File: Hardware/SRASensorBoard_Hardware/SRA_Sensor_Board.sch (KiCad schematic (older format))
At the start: 15 parts, among them U1 OKI-78SR-5_1.5-W36H-C, U2 OKI-78SR-3.3_1.5-W36H-C

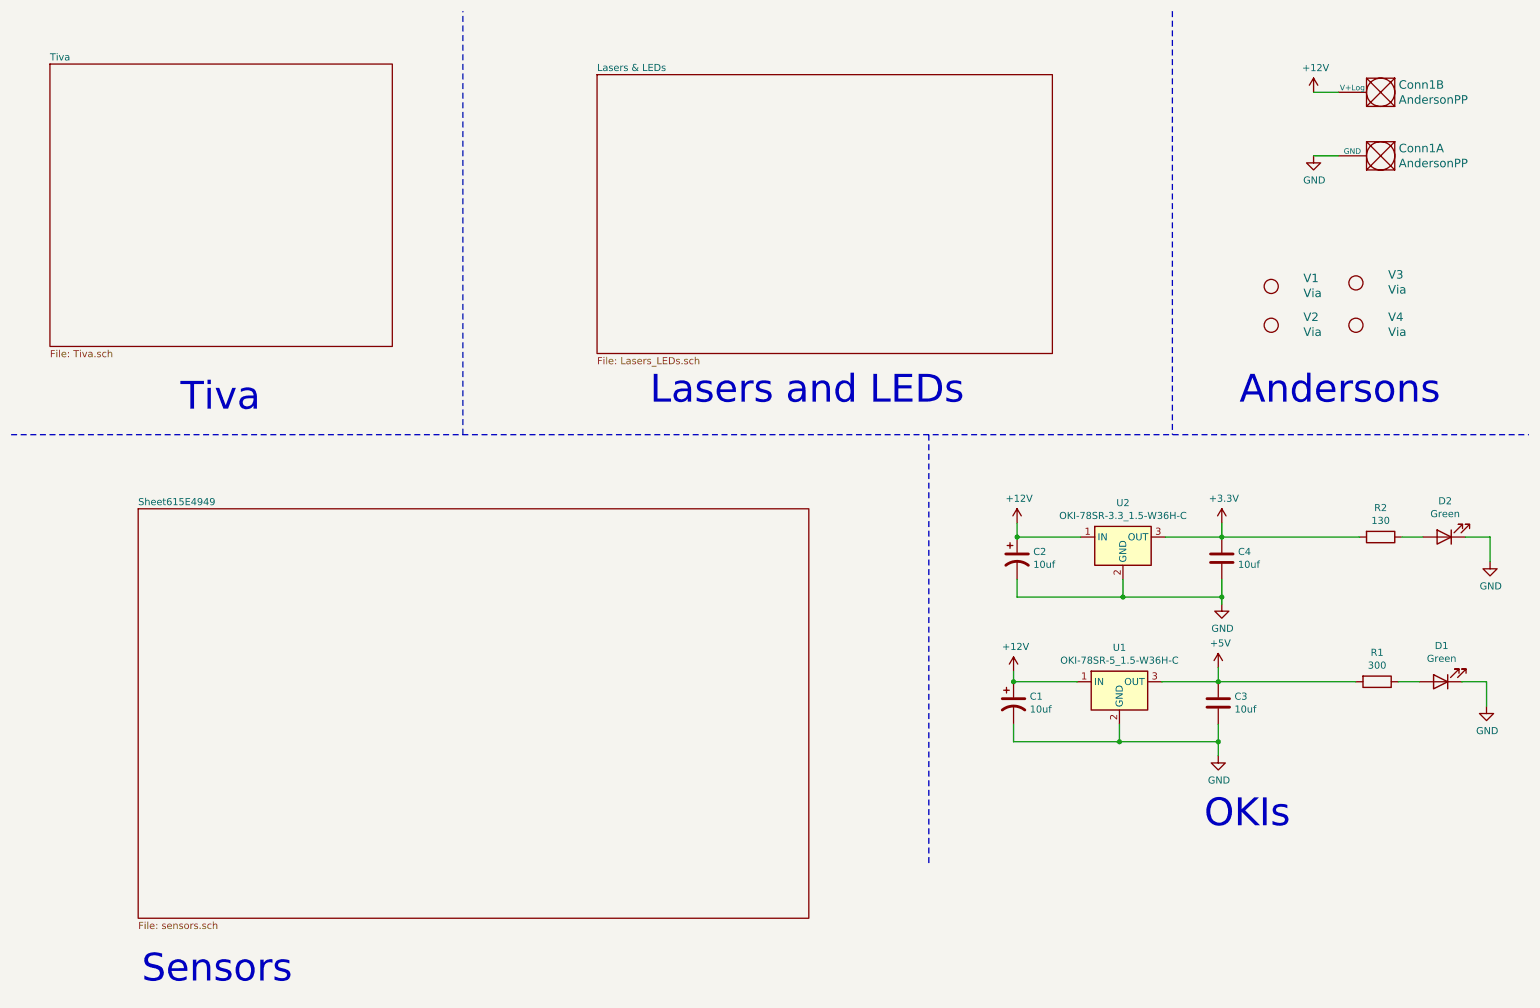
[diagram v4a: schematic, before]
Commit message: added teensy
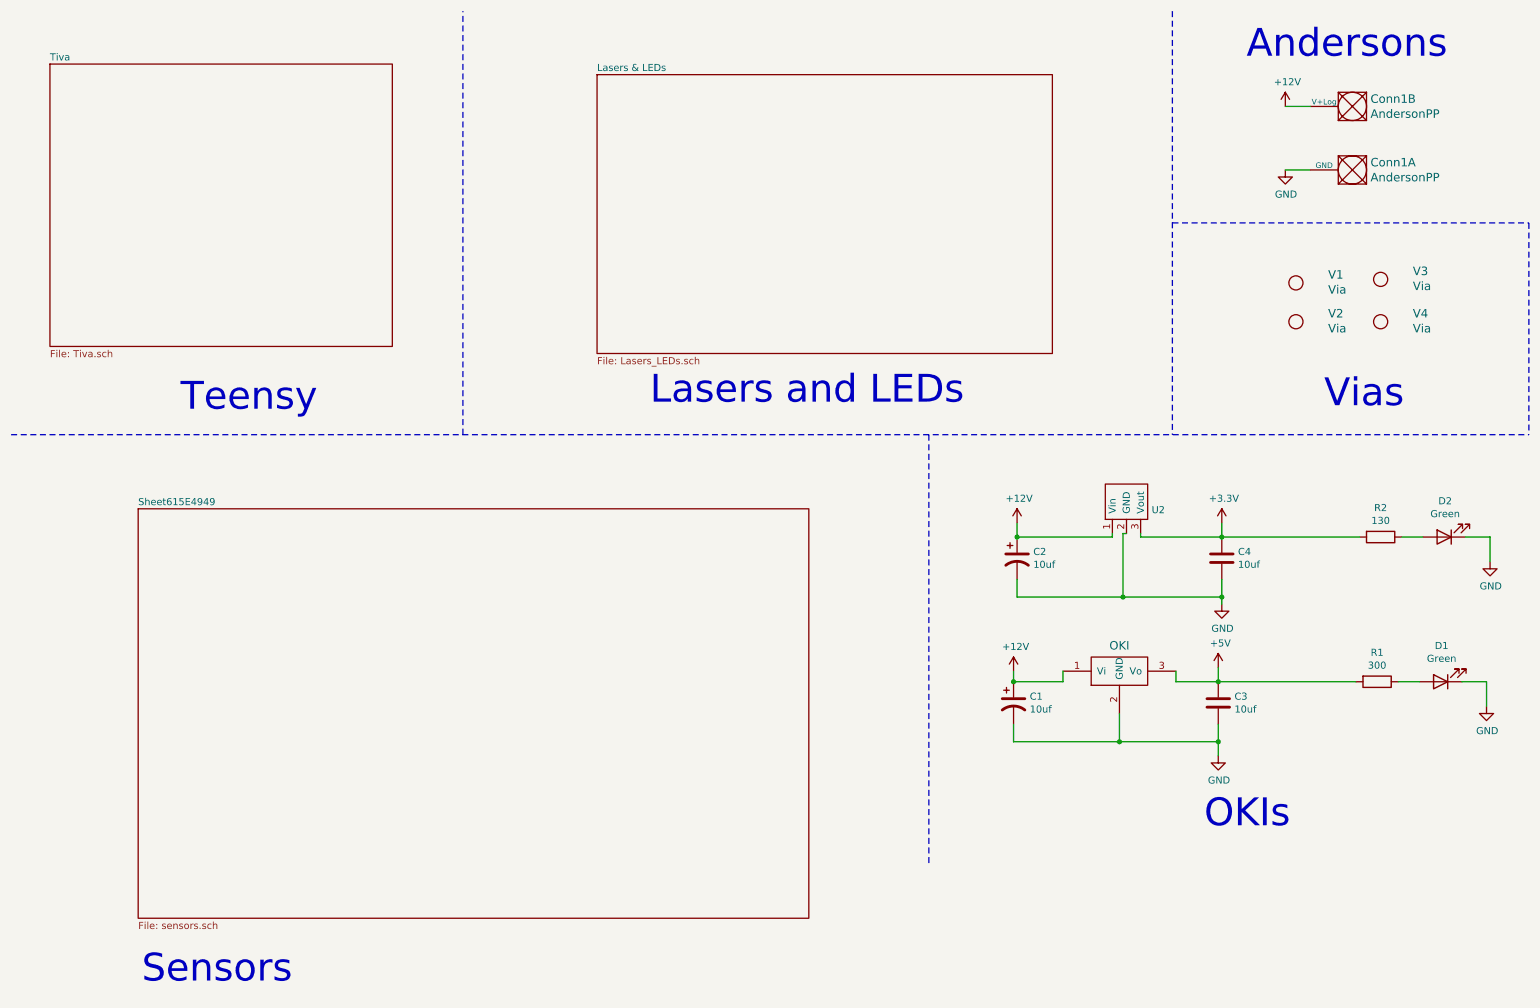
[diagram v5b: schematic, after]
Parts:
- removed U1: OKI-78SR-5_1.5-W36H-C, Converter_DCDC:Converter_DCDC_muRata_OKI-78SR_Horizontal, symbol Converter_DCDC:OKI-78SR-5_1.5-W36H-C
- removed U2: OKI-78SR-3.3_1.5-W36H-C, Converter_DCDC:Converter_DCDC_muRata_OKI-78SR_Horizontal, symbol Converter_DCDC:OKI-78SR-3.3_1.5-W36H-C
- added U1: OKI, MRDT_Devices:OKI_Horizontal, symbol MRDT_Devices:OKI
- added U2: TSR1-2433, MRDT_Devices:TSR_1-2433, symbol MRDT_Devices:TSR1-2433
- C2, C3, C4: footprint Capacitor_SMD:C_0603_1608Metric_Pad1.05x0.95mm_HandSolder -> Capacitor_SMD:C_0603_1608Metric_Pad1.08x0.95mm_HandSolder
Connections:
- net +12V: now also U1.1 (Vi), U2.1 (Vin)
- net +3V3: now also U2.3 (Vout)
- net +5V: now also U1.3 (Vo)
- net GND: now also U1.2 (GND), U2.2 (GND)
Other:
- note added: "Teensy"
- note added: "Vias"
- note removed: "Tiva"
- moved on the sheet: Conn1A, Conn1B, V1, V2, V3, V4
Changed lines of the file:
@@
 L MRDT_Connectors:AndersonPP Conn1
 U 2 1 614D19B3
-P 10275 950
-F 0 "Conn1" H 10247 997 60  0000 R CNN
-F 1 "AndersonPP" H 10247 1103 60  0000 R CNN
-F 2 "MRDT_Connectors:Anderson_2_Horizontal_Side_by_Side" H 10125 400 60  0001 C CNN
-F 3 "" H 10125 400 60  0001 C CNN
-	2    10275 950
+P 10075 1050
+F 0 "Conn1" H 10047 1097 60  0000 R CNN
+F 1 "AndersonPP" H 10047 1203 60  0000 R CNN
+F 2 "MRDT_Connectors:Anderson_2_Horizontal_Side_by_Side" H 9925 500 60  0001 C CNN
+F 3 "" H 9925 500 60  0001 C CNN
+	2    10075 1050
 	-1   0    0    1
 $EndComp
@@
 L MRDT_Connectors:AndersonPP Conn1
 U 1 1 614D22E6
-P 10275 1400
-F 0 "Conn1" H 10247 1447 60  0000 R CNN
-F 1 "AndersonPP" H 10247 1553 60  0000 R CNN
-F 2 "MRDT_Connectors:Anderson_2_Horizontal_Side_by_Side" H 10125 850 60  0001 C CNN
-F 3 "" H 10125 850 60  0001 C CNN
-	1    10275 1400
+P 10075 1500
+F 0 "Conn1" H 10047 1547 60  0000 R CNN
+F 1 "AndersonPP" H 10047 1653 60  0000 R CNN
+F 2 "MRDT_Connectors:Anderson_2_Horizontal_Side_by_Side" H 9925 950 60  0001 C CNN
+F 3 "" H 9925 950 60  0001 C CNN
+	1    10075 1500
 	-1   0    0    1
 $EndComp
@@
 	3675 3475 3675 475
 Text Notes 1675 3325 0    197  ~ 0
-Tiva
+Teensy
 Wire Notes Line
 	8700 475  8700 3475
-Text Notes 9175 3275 0    197  ~ 0
+Text Notes 9225 825  0    197  ~ 0
 Andersons
 Text Notes 8925 6275 0    197  ~ 0
@@
 	6975 3475 6975 6525
 $Comp
-L Converter_DCDC:OKI-78SR-5_1.5-W36H-C U1
-U 1 1 615099E1
-P 8325 5225
-F 0 "U1" H 8325 5467 50  0000 C CNN
-F 1 "OKI-78SR-5_1.5-W36H-C" H 8325 5376 50  0000 C CNN
-F 2 "Converter_DCDC:Converter_DCDC_muRata_OKI-78SR_Horizontal" H 8375 4975 50  0001 L CIN
-F 3 "https://power.murata.com/data/power/oki-78sr.pdf" H 8325 5225 50  0001 C CNN
-	1    8325 5225
-	1    0    0    -1
-$EndComp
-$Comp
-L Converter_DCDC:OKI-78SR-3.3_1.5-W36H-C U2
-U 1 1 61509405
-P 8350 4200
-F 0 "U2" H 8350 4442 50  0000 C CNN
-F 1 "OKI-78SR-3.3_1.5-W36H-C" H 8350 4351 50  0000 C CNN
-F 2 "Converter_DCDC:Converter_DCDC_muRata_OKI-78SR_Horizontal" H 8400 3950 50  0001 L CIN
-F 3 "https://power.murata.com/data/power/oki-78sr.pdf" H 8350 4200 50  0001 C CNN
-	1    8350 4200
-	1    0    0    -1
-$EndComp
-$Comp
 L Device:CP1 C2
 U 1 1 615E1386
@@
 F 0 "C2" H 7715 4396 50  0000 L CNN
 F 1 "10uf" H 7715 4305 50  0000 L CNN
-F 2 "Capacitor_SMD:C_0603_1608Metric_Pad1.05x0.95mm_HandSolder" H 7600 4350 50  0001 C CNN
+F 2 "Capacitor_SMD:C_0603_1608Metric_Pad1.08x0.95mm_HandSolder" H 7600 4350 50  0001 C CNN
 F 3 "~" H 7600 4350 50  0001 C CNN
 	1    7600 4350
@@
 F 0 "C4" H 9165 4396 50  0000 L CNN
 F 1 "10uf" H 9165 4305 50  0000 L CNN
-F 2 "Capacitor_SMD:C_0603_1608Metric_Pad1.05x0.95mm_HandSolder" H 9088 4200 50  0001 C CNN
+F 2 "Capacitor_SMD:C_0603_1608Metric_Pad1.08x0.95mm_HandSolder" H 9088 4200 50  0001 C CNN
 F 3 "~" H 9050 4350 50  0001 C CNN
 	1    9050 4350
@@
 $EndComp
 Wire Wire Line
-	7600 4200 8050 4200
-Wire Wire Line
 	7600 4500 7600 4625
 Wire Wire Line
 	7600 4625 8350 4625
-Wire Wire Line
-	8350 4625 8350 4500
 Wire Wire Line
 	9050 4625 9050 4500
@@
 Wire Wire Line
 	10950 4200 10950 4375
-Wire Wire Line
-	8650 4200 9050 4200
 $Comp
 L Device:CP1 C1
@@
 F 0 "C3" H 9140 5421 50  0000 L CNN
 F 1 "10uf" H 9140 5330 50  0000 L CNN
-F 2 "Capacitor_SMD:C_0603_1608Metric_Pad1.05x0.95mm_HandSolder" H 9063 5225 50  0001 C CNN
+F 2 "Capacitor_SMD:C_0603_1608Metric_Pad1.08x0.95mm_HandSolder" H 9063 5225 50  0001 C CNN
 F 3 "~" H 9025 5375 50  0001 C CNN
 	1    9025 5375
@@
 $EndComp
 Wire Wire Line
-	7575 5225 8025 5225
+	7575 5225 7925 5225
 Wire Wire Line
 	7575 5525 7575 5650
 Wire Wire Line
 	7575 5650 8325 5650
-Wire Wire Line
-	8325 5650 8325 5525
 Wire Wire Line
 	9025 5650 9025 5525
@@
 Wire Wire Line
 	10925 5225 10925 5400
-Wire Wire Line
-	8625 5225 9025 5225
 $Comp
 L power:+12V #PWR0103
 U 1 1 615F977E
-P 9700 1050
-F 0 "#PWR0103" H 9700 900 50  0001 C CNN
-F 1 "+12V" H 9715 1223 50  0000 C CNN
-F 2 "" H 9700 1050 50  0001 C CNN
-F 3 "" H 9700 1050 50  0001 C CNN
-	1    9700 1050
+P 9500 1150
+F 0 "#PWR0103" H 9500 1000 50  0001 C CNN
+F 1 "+12V" H 9515 1323 50  0000 C CNN
+F 2 "" H 9500 1150 50  0001 C CNN
+F 3 "" H 9500 1150 50  0001 C CNN
+	1    9500 1150
 	1    0    0    -1
 $EndComp
@@
 L power:GND #PWR0104
 U 1 1 615FA471
-P 9700 1500
-F 0 "#PWR0104" H 9700 1250 50  0001 C CNN
-F 1 "GND" H 9705 1327 50  0000 C CNN
-F 2 "" H 9700 1500 50  0001 C CNN
-F 3 "" H 9700 1500 50  0001 C CNN
-	1    9700 1500
-	1    0    0    -1
-$EndComp
-Wire Wire Line
-	9700 1500 9875 1500
-Wire Wire Line
-	9875 1050 9700 1050
+P 9500 1600
+F 0 "#PWR0104" H 9500 1350 50  0001 C CNN
+F 1 "GND" H 9505 1427 50  0000 C CNN
+F 2 "" H 9500 1600 50  0001 C CNN
+F 3 "" H 9500 1600 50  0001 C CNN
+	1    9500 1600
+	1    0    0    -1
+$EndComp
+Wire Wire Line
+	9500 1600 9675 1600
+Wire Wire Line
+	9675 1150 9500 1150
 $Sheet
 S 1375 4000 4750 2900
@@
 L MRDT_Drill_Holes:Via V2
 U 1 1 622C1FEF
-P 9400 2700
-F 0 "V2" H 9628 2758 60  0000 L CNN
-F 1 "Via" H 9628 2652 60  0000 L CNN
-F 2 "MRDT_Drill_Holes:4_40_Hole_Corner" H 9400 2700 60  0001 C CNN
-F 3 "" H 9400 2700 60  0001 C CNN
-	1    9400 2700
+P 9575 2675
+F 0 "V2" H 9803 2733 60  0000 L CNN
+F 1 "Via" H 9803 2627 60  0000 L CNN
+F 2 "MRDT_Drill_Holes:4_40_Hole_Corner" H 9575 2675 60  0001 C CNN
+F 3 "" H 9575 2675 60  0001 C CNN
+	1    9575 2675
 	1    0    0    -1
 $EndComp
@@
 L MRDT_Drill_Holes:Via V1
 U 1 1 622C2C38
-P 9400 2425
-F 0 "V1" H 9628 2483 60  0000 L CNN
-F 1 "Via" H 9628 2377 60  0000 L CNN
-F 2 "MRDT_Drill_Holes:4_40_Hole_Corner" H 9400 2425 60  0001 C CNN
-F 3 "" H 9400 2425 60  0001 C CNN
-	1    9400 2425
+P 9575 2400
+F 0 "V1" H 9803 2458 60  0000 L CNN
+F 1 "Via" H 9803 2352 60  0000 L CNN
+F 2 "MRDT_Drill_Holes:4_40_Hole_Corner" H 9575 2400 60  0001 C CNN
+F 3 "" H 9575 2400 60  0001 C CNN
+	1    9575 2400
 	1    0    0    -1
 $EndComp
@@
 L MRDT_Drill_Holes:Via V3
 U 1 1 622C343B
-P 10000 2400
-F 0 "V3" H 10228 2458 60  0000 L CNN
-F 1 "Via" H 10228 2352 60  0000 L CNN
-F 2 "MRDT_Drill_Holes:4_40_Hole_Corner" H 10000 2400 60  0001 C CNN
-F 3 "" H 10000 2400 60  0001 C CNN
-	1    10000 2400
+P 10175 2375
+F 0 "V3" H 10403 2433 60  0000 L CNN
+F 1 "Via" H 10403 2327 60  0000 L CNN
+F 2 "MRDT_Drill_Holes:4_40_Hole_Corner" H 10175 2375 60  0001 C CNN
+F 3 "" H 10175 2375 60  0001 C CNN
+	1    10175 2375
 	1    0    0    -1
 $EndComp
@@
 L MRDT_Drill_Holes:Via V4
 U 1 1 622C3B50
-P 10000 2700
-F 0 "V4" H 10228 2758 60  0000 L CNN
-F 1 "Via" H 10228 2652 60  0000 L CNN
-F 2 "MRDT_Drill_Holes:4_40_Hole_Corner" H 10000 2700 60  0001 C CNN
-F 3 "" H 10000 2700 60  0001 C CNN
-	1    10000 2700
-	1    0    0    -1
-$EndComp
+P 10175 2675
+F 0 "V4" H 10403 2733 60  0000 L CNN
+F 1 "Via" H 10403 2627 60  0000 L CNN
+F 2 "MRDT_Drill_Holes:4_40_Hole_Corner" H 10175 2675 60  0001 C CNN
+F 3 "" H 10175 2675 60  0001 C CNN
+	1    10175 2675
+	1    0    0    -1
+$EndComp
+Wire Notes Line
+	11225 1975 11225 3475
+Wire Notes Line
+	8700 1975 11225 1975
+Text Notes 9775 3300 0    197  ~ 0
+Vias
+$Comp
+L MRDT_Devices:TSR1-2433 U2
+U 1 1 6234DDBD
+P 8375 4175
+F 0 "U2" V 8542 3997 50  0000 R CNN
+F 1 "TSR1-2433" V 8775 4175 50  0001 C CNN
+F 2 "MRDT_Devices:TSR_1-2433" H 8675 4275 50  0001 C CNN
+F 3 "" H 8675 4275 50  0001 C CNN
+	1    8375 4175
+	0    -1   -1   0
+$EndComp
+Wire Wire Line
+	8275 4200 8275 4175
+Wire Wire Line
+	7600 4200 8275 4200
+Wire Wire Line
+	8475 4200 8475 4175
+Wire Wire Line
+	8475 4200 9050 4200
+Wire Wire Line
+	8350 4175 8375 4175
+Wire Wire Line
+	8350 4175 8350 4625
+Wire Wire Line
+	8325 5450 8325 5650
+Wire Wire Line
+	8725 5225 8725 5150
+Wire Wire Line
+	8725 5225 9025 5225
+Wire Wire Line
+	7925 5150 7925 5225
+$Comp
+L MRDT_Devices:OKI U1
+U 1 1 6235BB5C
+P 8125 5250
+F 0 "U1" H 8175 5200 60  0001 C CNN
+F 1 "OKI" H 8325 5531 60  0000 C CNN
+F 2 "MRDT_Devices:OKI_Horizontal" H 7925 5150 60  0001 C CNN
+F 3 "" H 7925 5150 60  0001 C CNN
+	1    8125 5250
+	1    0    0    -1
+$EndComp
